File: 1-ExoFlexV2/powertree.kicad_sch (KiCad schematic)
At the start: 54 parts, among them J5 Jumper, J6 Jumper, J7 Jumper 5,2A, J71 Jumper 5,2A, J8 USB-C, J81 14 AWG, U123 LDO -5VA, U124 LDO 5VA, U14 TVS 24V, U5 DCDC24V/8V, U6 DCDC24V/5V NUM, U7 DCDC 24V/-7,8V ANA

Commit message: PLacement 2
- Puissance
- signaux
-
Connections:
- net GND: now also U7.5 (GND); no longer U7.P5 (GND)
- net at C11.1, C12.2, R7.1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: now also U7.1 (VOUT); no longer U7.P1 (VOUT)
- net at C5.1, C7.1, C8.1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: now also U7.2 (VIN); no longer U7.P2 (VIN)
- net at R7.2: now also U7.4 (SET); no longer U7.P4 (SET)
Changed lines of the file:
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@@
       (effects (font (size 1.27 1.27)) hide)
     )
-    (pin "P1")
-    (pin "P2")
-    (pin "P3")
-    (pin "P4")
-    (pin "P5")
+    (pin "1")
+    (pin "2")
+    (pin "3")
+    (pin "4")
+    (pin "5")
   )
   (symbol (lib_id "Device:C") (at 35.56 46.99 0) (unit 1)
@@
     (pin "3")
   )
-  (symbol (lib_id "Device:C") (at 57.15 137.16 0) (unit 1)
+  (symbol (lib_id "Device:C") (at 57.15 137.16 0) (mirror y) (unit 1)
     (in_bom yes) (on_board yes)
-    (property "Reference" "C8" (id 0) (at 53.34 134.62 0)
+    (property "Reference" "C8" (id 0) (at 60.96 134.62 0)
       (effects (font (size 1.27 1.27)) (justify left))
     )
-    (property "Value" "4,7uF 35V X7R" (id 1) (at 59.69 143.51 0)
+    (property "Value" "4,7uF 35V X7R" (id 1) (at 54.61 143.51 0)
       (effects (font (size 1.27 1.27)) (justify left) hide)
     )
-    (property "Footprint" "Capacitor_SMD:C_0805_2012Metric" (id 2) (at 58.1152 140.97 0)
+    (property "Footprint" "Capacitor_SMD:C_0805_2012Metric" (id 2) (at 56.1848 140.97 0)
       (effects (font (size 1.27 1.27)) hide)
     )

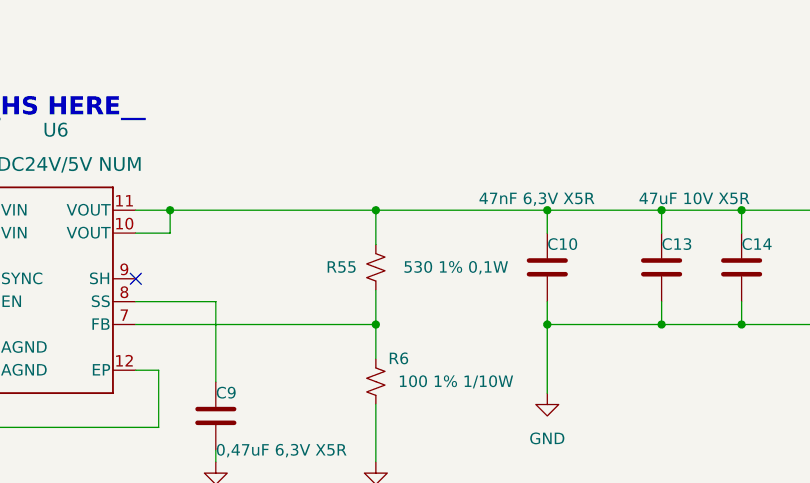
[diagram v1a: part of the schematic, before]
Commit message: Routage Fin
- Alimentation router
- Urg Sec dans le OR gate vers Alim Sec
- Changement d'un condo
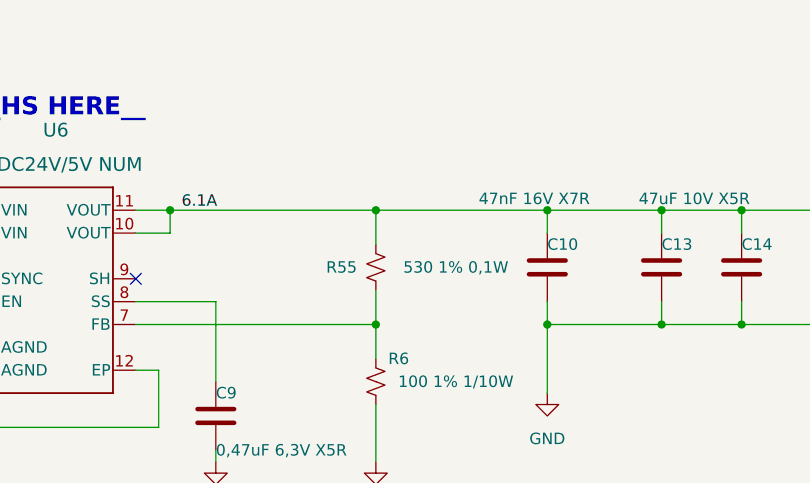
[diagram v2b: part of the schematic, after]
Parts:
- C10: value 47nF 6,3V X5R -> 47nF 16V X7R; footprint Capacitor_SMD:C_01005_0402Metric -> Capacitor_SMD:C_0603_1608Metric; DESCRIPTION 0.047 µF ±20% 6.3V Ceramic Capacitor X5R 01005 (0402 Metric) -> 0.047 µF ±20% 16V Ceramic Capacitor X7R 0603 (1608 Metric); MANUFACTURER Murata Electronics -> Johanson Dielectrics Inc.; PACKAGE 01005 (0402 Metric) -> 0603 (1608 Metric; PART NUMBER GRM022R60J473ME15L -> EMCP160W473M1GV001T
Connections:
- net 6.1A: now reaches C10.1, C13.1, C14.1, C15.1, C16.1, J7.2 (Pin_2), J71.2 (Pin_2), R185.2, R55.2, TP9.TP, U14.3 (IO), U6.10 (VOUT), U6.11 (VOUT)
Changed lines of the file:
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@@
     (effects (font (size 2.25 2.25) (thickness 0.45) bold) (justify left bottom))
+  )
+  (label "6.1A" (at 80.01 36.83 0)
+    (effects (font (size 1.27 1.27)) (justify left bottom))
   )
   (symbol (lib_id "SymLib:PTN78060WAD") (at 66.04 91.44 0) (unit 1)
@@
       (effects (font (size 1.27 1.27)) (justify left))
     )
-    (property "Value" "47nF 6,3V X5R" (id 1) (at 113.03 35.56 0)
-      (effects (font (size 1.27 1.27)) (justify left))
-    )
-    (property "Footprint" "Capacitor_SMD:C_01005_0402Metric" (id 2) (at 121.6152 46.99 0)
+    (property "Value" "47nF 16V X7R" (id 1) (at 113.03 35.56 0)
+      (effects (font (size 1.27 1.27)) (justify left))
+    )
+    (property "Footprint" "Capacitor_SMD:C_0603_1608Metric" (id 2) (at 121.6152 46.99 0)
       (effects (font (size 1.27 1.27)) hide)
     )
@@
       (effects (font (size 1.27 1.27)) hide)
     )
-    (property "MANUFACTURER" "Murata Electronics" (id 4) (at 120.65 43.18 0)
-      (effects (font (size 1.27 1.27)) hide)
-    )
-    (property "PACKAGE" "01005 (0402 Metric)" (id 5) (at 120.65 43.18 0)
-      (effects (font (size 1.27 1.27)) hide)
-    )
-    (property "PART NUMBER" "GRM022R60J473ME15L" (id 6) (at 120.65 43.18 0)
+    (property "MANUFACTURER" "Johanson Dielectrics Inc." (id 4) (at 120.65 43.18 0)
+      (effects (font (size 1.27 1.27)) hide)
+    )
+    (property "PACKAGE" "0603 (1608 Metric" (id 5) (at 120.65 43.18 0)
+      (effects (font (size 1.27 1.27)) hide)
+    )
+    (property "PART NUMBER" "EMCP160W473M1GV001T" (id 6) (at 120.65 43.18 0)
       (effects (font (size 1.27 1.27)) hide)
     )
@@
       (effects (font (size 1.27 1.27)) hide)
     )
-    (property "DESCRIPTION" "0.047 µF ±20% 6.3V Ceramic Capacitor X5R 01005 (0402 Metric)" (id 8) (at 120.65 43.18 0)
-      (effects (font (size 1.27 1.27)) hide)
-    )
+    (property "DESCRIPTION" "0.047 µF ±20% 16V Ceramic Capacitor X7R 0603 (1608 Metric)" (id 8) (at 120.65 43.18 0)
+      (effects (font (size 1.27 1.27)) hide)
+    )

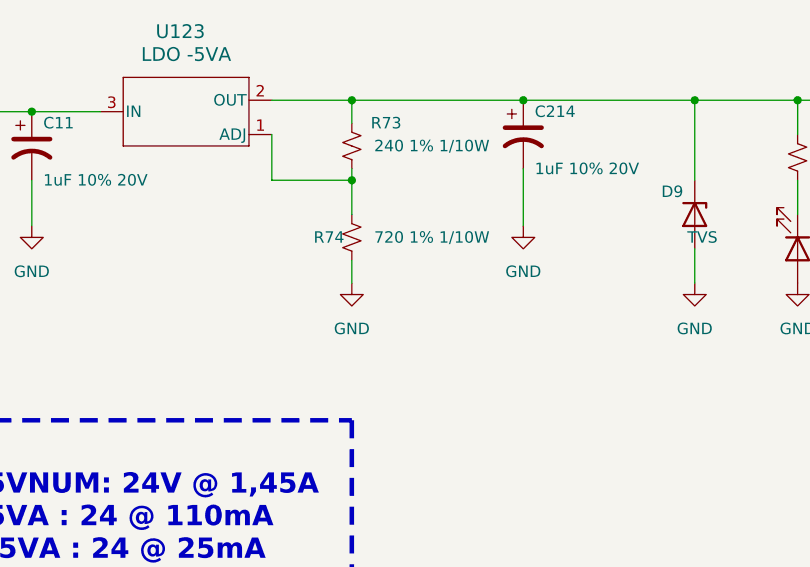
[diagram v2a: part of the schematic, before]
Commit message: Routage pour Review 1
- Replacement des test point pour faciliter le rework
- Correction des erreurs dans le BOM
-
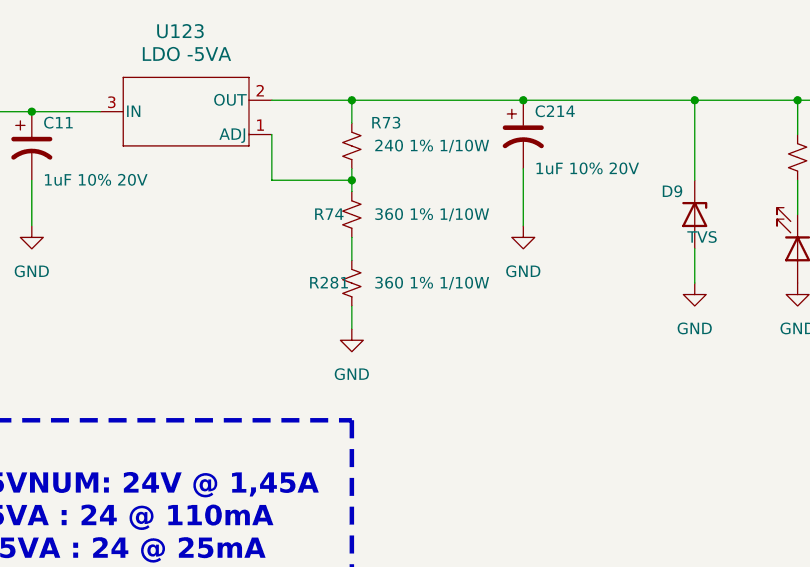
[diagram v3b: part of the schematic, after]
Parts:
- added R281: 360 1% 1/10W, Resistor_SMD:R_0603_1608Metric, symbol Device:R_Small_US
- R74: value 720 1% 1/10W -> 360 1% 1/10W; DESCRIPTION 720 Ohms ±1% 0.1W, 1/10W Chip Resistor 0603 (1608 Metric) A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 -> 360 Ohms ±1% 0.1W, 1/10W Chip Resistor 0603 (1608 Metric) A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; MANUFACTURER Vishay Dale -> Panasonic Electronic Components; PART NUMBER CRCW0603720RFKTA -> ERJ-3EKF3600V
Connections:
- net GND: now also R281.1; no longer R74.1
- new net: R281.2, R74.1
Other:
- moved on the sheet: R74
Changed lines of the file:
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@@
+    (stroke (width 0) (type default) (color 0 0 0 0))
+  )
+  (wire (pts (xy 165.1 151.13) (xy 165.1 153.67))
     (stroke (width 0) (type default) (color 0 0 0 0))
   )
@@
     (stroke (width 0) (type default) (color 0 0 0 0))
   )
-  (wire (pts (xy 165.1 146.05) (xy 165.1 148.59))
+  (wire (pts (xy 165.1 143.51) (xy 165.1 146.05))
     (stroke (width 0) (type default) (color 0 0 0 0))
   )
@@
     (stroke (width 0) (type default) (color 0 0 0 0))
   )
-  (wire (pts (xy 165.1 137.16) (xy 165.1 140.97))
+  (wire (pts (xy 165.1 137.16) (xy 165.1 138.43))
     (stroke (width 0) (type default) (color 0 0 0 0))
   )
@@
     (pin "1")
   )
-  (symbol (lib_id "Device:R_Small_US") (at 165.1 143.51 180) (unit 1)
-    (in_bom yes) (on_board yes)
-    (property "Reference" "R74" (id 0) (at 162.56 143.51 0))
-    (property "Value" "720 1% 1/10W" (id 1) (at 173.99 143.51 0))
-    (property "Footprint" "Resistor_SMD:R_0603_1608Metric" (id 2) (at 165.1 143.51 0)
-      (effects (font (size 1.27 1.27)) hide)
-    )
-    (property "Datasheet" "~" (id 3) (at 165.1 143.51 0)
-      (effects (font (size 1.27 1.27)) hide)
-    )
-    (property "MANUFACTURER" "Vishay Dale" (id 4) (at 165.1 143.51 0)
-      (effects (font (size 1.27 1.27)) hide)
-    )
-    (property "PACKAGE" "0603 (1608 Metric)" (id 5) (at 165.1 143.51 0)
-      (effects (font (size 1.27 1.27)) hide)
-    )
-    (property "PART NUMBER" "CRCW0603720RFKTA" (id 6) (at 165.1 143.51 0)
-      (effects (font (size 1.27 1.27)) hide)
-    )
-    (property "TYPE" "SMD" (id 7) (at 165.1 143.51 0)
-      (effects (font (size 1.27 1.27)) hide)
-    )
-    (property "DESCRIPTION" "720 Ohms ±1% 0.1W, 1/10W Chip Resistor 0603 (1608 Metric) Automotive AEC-Q200 Thick Film" (id 8) (at 165.1 143.51 0)
+  (symbol (lib_id "Device:R_Small_US") (at 165.1 140.97 180) (unit 1)
+    (in_bom yes) (on_board yes)
+    (property "Reference" "R74" (id 0) (at 162.56 140.97 0))
+    (property "Value" "360 1% 1/10W " (id 1) (at 173.99 140.97 0))
+    (property "Footprint" "Resistor_SMD:R_0603_1608Metric" (id 2) (at 165.1 140.97 0)
+      (effects (font (size 1.27 1.27)) hide)
+    )
+    (property "Datasheet" "~" (id 3) (at 165.1 140.97 0)
+      (effects (font (size 1.27 1.27)) hide)
+    )
+    (property "MANUFACTURER" "Panasonic Electronic Components" (id 4) (at 165.1 140.97 0)
+      (effects (font (size 1.27 1.27)) hide)
+    )
+    (property "PACKAGE" "0603 (1608 Metric)" (id 5) (at 165.1 140.97 0)
+      (effects (font (size 1.27 1.27)) hide)
+    )
+    (property "PART NUMBER" "ERJ-3EKF3600V" (id 6) (at 165.1 140.97 0)
+      (effects (font (size 1.27 1.27)) hide)
+    )
+    (property "TYPE" "SMD" (id 7) (at 165.1 140.97 0)
+      (effects (font (size 1.27 1.27)) hide)
+    )
+    (property "DESCRIPTION" "360 Ohms ±1% 0.1W, 1/10W Chip Resistor 0603 (1608 Metric) Automotive AEC-Q200 Thick Film" (id 8) (at 165.1 140.97 0)
       (effects (font (size 1.27 1.27)) hide)
     )
@@
     (pin "1")
   )
+  (symbol (lib_id "Device:R_Small_US") (at 165.1 148.59 180) (unit 1)
+    (in_bom yes) (on_board yes)
+    (property "Reference" "R281" (id 0) (at 162.56 148.59 0))
+    (property "Value" "360 1% 1/10W " (id 1) (at 173.99 148.59 0))
+    (property "Footprint" "Resistor_SMD:R_0603_1608Metric" (id 2) (at 165.1 148.59 0)
+      (effects (font (size 1.27 1.27)) hide)
+    )
+    (property "Datasheet" "~" (id 3) (at 165.1 148.59 0)
+      (effects (font (size 1.27 1.27)) hide)
+    )
+    (property "MANUFACTURER" "Panasonic Electronic Components" (id 4) (at 165.1 148.59 0)
+      (effects (font (size 1.27 1.27)) hide)
+    )
+    (property "PACKAGE" "0603 (1608 Metric)" (id 5) (at 165.1 148.59 0)
+      (effects (font (size 1.27 1.27)) hide)
+    )
+    (property "PART NUMBER" "ERJ-3EKF3600V" (id 6) (at 165.1 148.59 0)
+      (effects (font (size 1.27 1.27)) hide)
+    )
+    (property "TYPE" "SMD" (id 7) (at 165.1 148.59 0)
+      (effects (font (size 1.27 1.27)) hide)
+    )
+    (property "DESCRIPTION" "360 Ohms ±1% 0.1W, 1/10W Chip Resistor 0603 (1608 Metric) Automotive AEC-Q200 Thick Film" (id 8) (at 165.1 148.59 0)
+      (effects (font (size 1.27 1.27)) hide)
+    )
+    (pin "1")
+    (pin "2")
+  )
   (symbol (lib_id "SymLib:1729128") (at 241.3 102.87 0) (unit 1)
     (in_bom yes) (on_board yes)
@@
     (pin "1")
   )
-  (symbol (lib_id "power:GND") (at 165.1 148.59 0) (unit 1)
-    (in_bom yes) (on_board yes) (fields_autoplaced)
-    (property "Reference" "#PWR0100" (id 0) (at 165.1 154.94 0)
-      (effects (font (size 1.27 1.27)) hide)
-    )
-    (property "Value" "GND" (id 1) (at 165.1 153.67 0))
-    (property "Footprint" "" (id 2) (at 165.1 148.59 0)
-      (effects (font (size 1.27 1.27)) hide)
-    )
-    (property "Datasheet" "" (id 3) (at 165.1 148.59 0)
-      (effects (font (size 1.27 1.27)) hide)
-    )
+  (symbol (lib_id "power:GND") (at 165.1 153.67 0) (unit 1)
+    (in_bom yes) (on_board yes) (fields_autoplaced)
+    (property "Reference" "#PWR0100" (id 0) (at 165.1 160.02 0)
+      (effects (font (size 1.27 1.27)) hide)
+    )
+    (property "Value" "GND" (id 1) (at 165.1 158.75 0))
+    (property "Footprint" "" (id 2) (at 165.1 153.67 0)
+      (effects (font (size 1.27 1.27)) hide)
+    )
+    (property "Datasheet" "" (id 3) (at 165.1 153.67 0)
+      (effects (font (size 1.27 1.27)) hide)
+    )
